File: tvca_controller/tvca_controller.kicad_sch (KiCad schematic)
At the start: 32 parts, among them J1 Programming Header, J2 CAN connector, J3 Batt, J8 Batt, U1 PIC18F26K83, U2 MCP2562, U3 INA180, Y1 Crystal

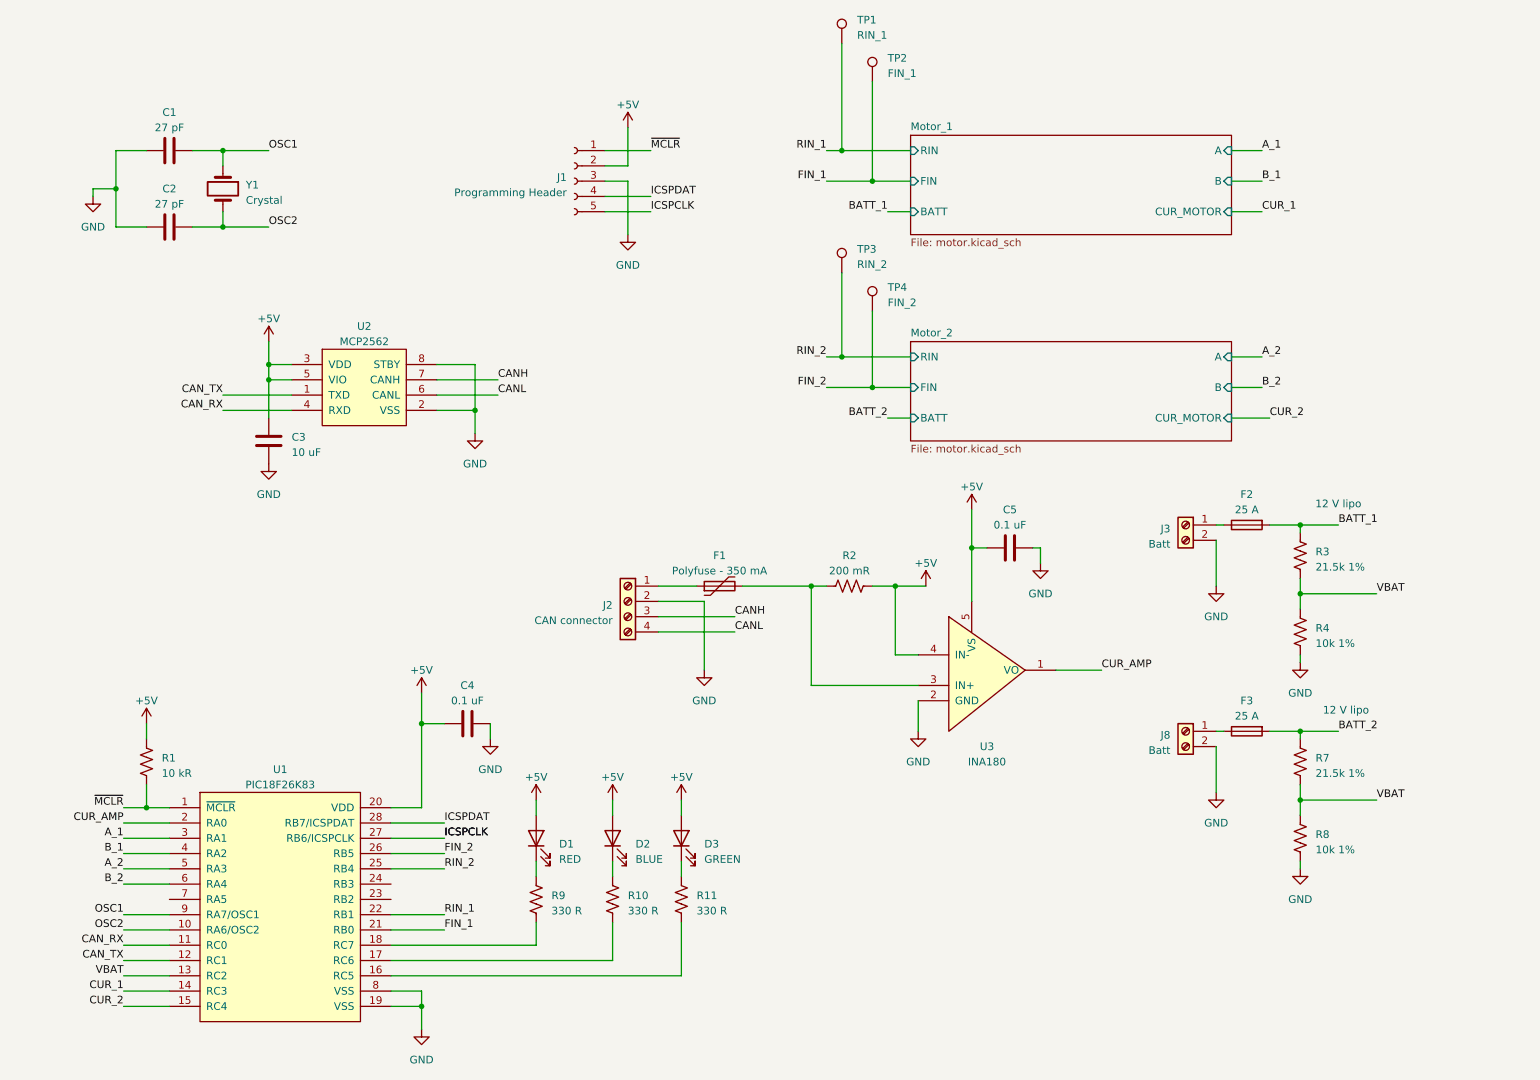
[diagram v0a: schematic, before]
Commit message: Replace motor controller IC
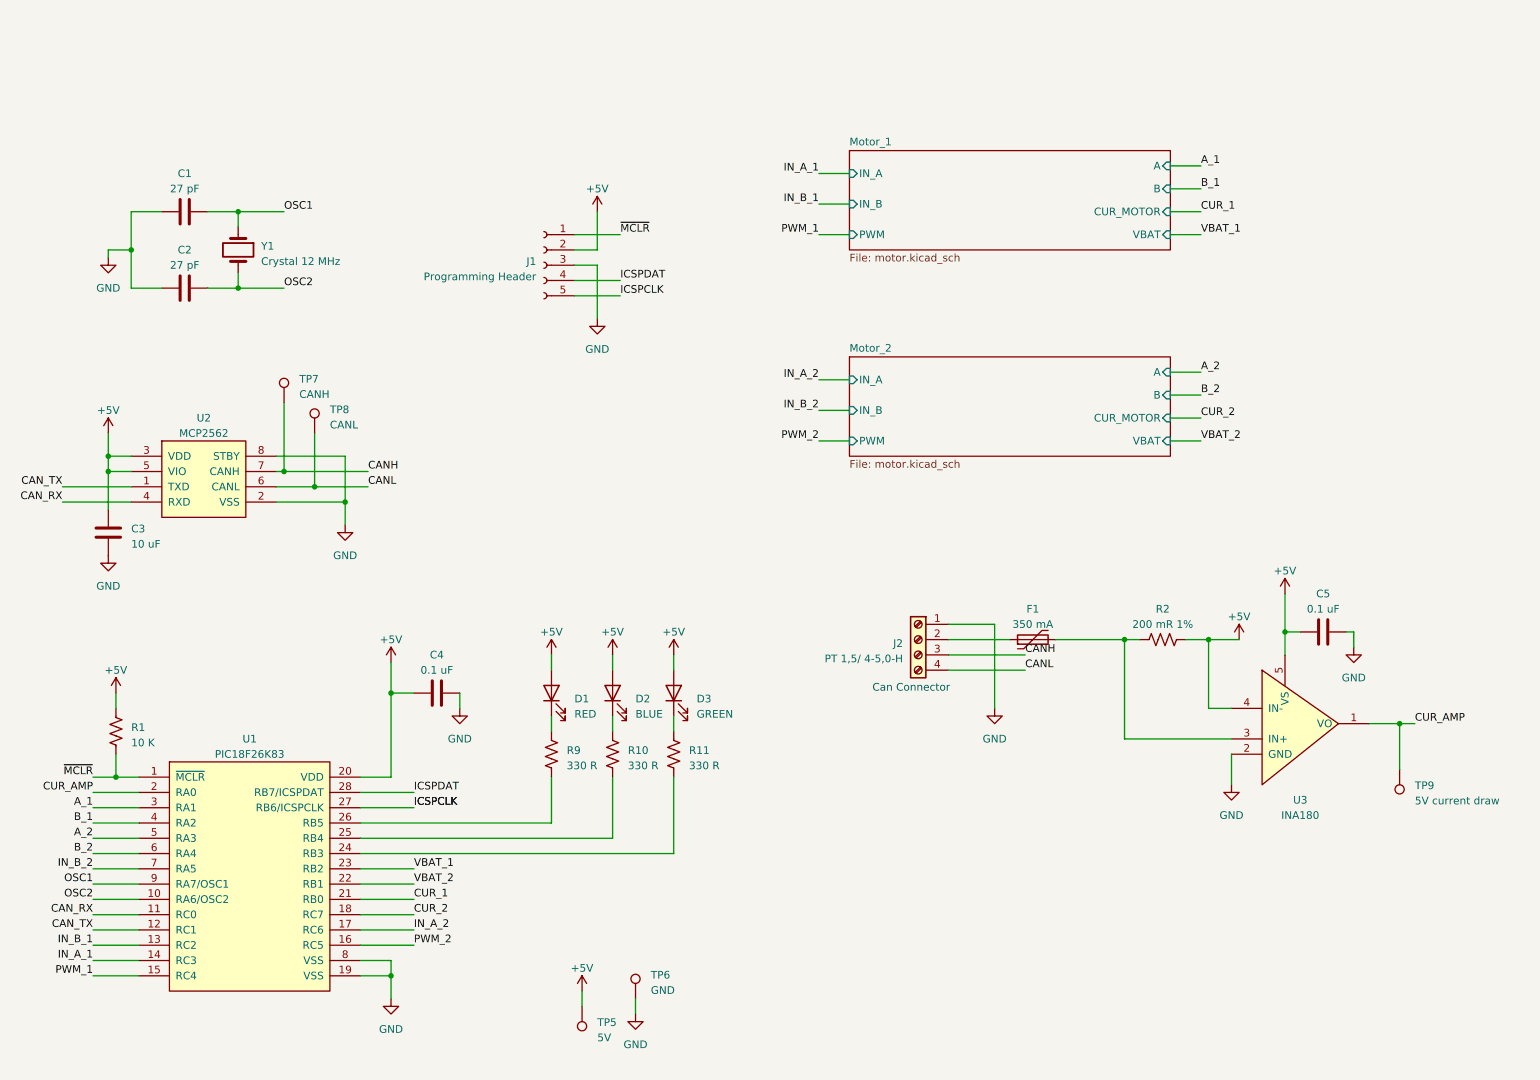
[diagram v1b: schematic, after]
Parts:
- removed F2, F3: 25 A, Fuse:Fuseholder_Cylinder-6.3x32mm_Schurter_0031-8002_Horizontal_Open, symbol Device:Fuse
- removed J3, J8: Batt, canhw_footprints:TE_2-1437667-4, symbol Connector:Screw_Terminal_01x02
- removed R3, R7: 21.5k 1%, Resistor_SMD:R_0805_2012Metric_Pad1.20x1.40mm_HandSolder, symbol Device:R_US
- removed R4, R8: 10k 1%, Resistor_SMD:R_0805_2012Metric_Pad1.20x1.40mm_HandSolder, symbol Device:R_US
- removed TP1: RIN_1, TestPoint:TestPoint_THTPad_2.5x2.5mm_Drill1.2mm, symbol Connector:TestPoint
- removed TP2: FIN_1, TestPoint:TestPoint_THTPad_2.5x2.5mm_Drill1.2mm, symbol Connector:TestPoint
- removed TP3: RIN_2, TestPoint:TestPoint_THTPad_2.5x2.5mm_Drill1.2mm, symbol Connector:TestPoint
- removed TP4: FIN_2, TestPoint:TestPoint_THTPad_2.5x2.5mm_Drill1.2mm, symbol Connector:TestPoint
- added TP5: 5V, TestPoint:TestPoint_THTPad_2.5x2.5mm_Drill1.2mm, symbol Connector:TestPoint
- added TP6: GND, TestPoint:TestPoint_THTPad_2.5x2.5mm_Drill1.2mm, symbol Connector:TestPoint
- added TP7: CANH, TestPoint:TestPoint_THTPad_2.5x2.5mm_Drill1.2mm, symbol Connector:TestPoint
- added TP8: CANL, TestPoint:TestPoint_THTPad_2.5x2.5mm_Drill1.2mm, symbol Connector:TestPoint
- added TP9: 5V current draw, TestPoint:TestPoint_THTPad_2.5x2.5mm_Drill1.2mm, symbol Connector:TestPoint
- F1: value Polyfuse - 350 mA -> 350 mA
- J2: value CAN connector -> PT 1,5/ 4-5,0-H
- R1: value 10 kR -> 10 K
- R2: value 200 mR -> 200 mR 1%
- Y1: value Crystal -> Crystal 12 MHz
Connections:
- net FIN_1 is gone; now on net CUR_1: U1.21 (RB0)
- net FIN_2 is gone; now on an unnamed net: U1.26 (RB5)
- net RIN_2 is gone; now on an unnamed net: U1.25 (RB4)
- net +5V: now also TP5.1
- net CANH: now also TP7.1
- net CANL: now also TP8.1
- net CUR_1: no longer U1.14 (RC3)
- net CUR_2: now also U1.18 (RC7); no longer U1.15 (RC4)
- net CUR_AMP: now also TP9.1
- net GND: now also J2.1 (Pin_1), TP6.1; no longer J2.2 (Pin_2)
- net at F1.1: now also J2.2 (Pin_2); no longer J2.1 (Pin_1)
- net at R9.1: no longer U1.18 (RC7)
- net at R11.1: now also U1.24 (RB3); no longer U1.16 (RC5)
- net at R10.1: no longer U1.17 (RC6)
- net VBAT_1: now reaches U1.23 (RB2)
- net IN_B_2: now reaches U1.7 (RA5)
- net RIN_1 renamed VBAT_2
- net VBAT renamed IN_B_1
- new net IN_A_1: U1.14 (RC3)
- new net IN_A_2: U1.17 (RC6)
- new net PWM_1: U1.15 (RC4)
- new net PWM_2: U1.16 (RC5)
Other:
- sheet Motor_1 ports: added IN_A, IN_B, PWM, VBAT; removed BATT, FIN, RIN
- sheet Motor_2 ports: added IN_A, IN_B, PWM, VBAT; removed BATT, FIN, RIN
- note added: "Can Connector"
- note removed: "12 V lipo"
- moved on the sheet: C1, C2, C3, C4, C5, D1, D2, D3, J1, J2, R1, R10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

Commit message: Update motor controller IC and fuse holders
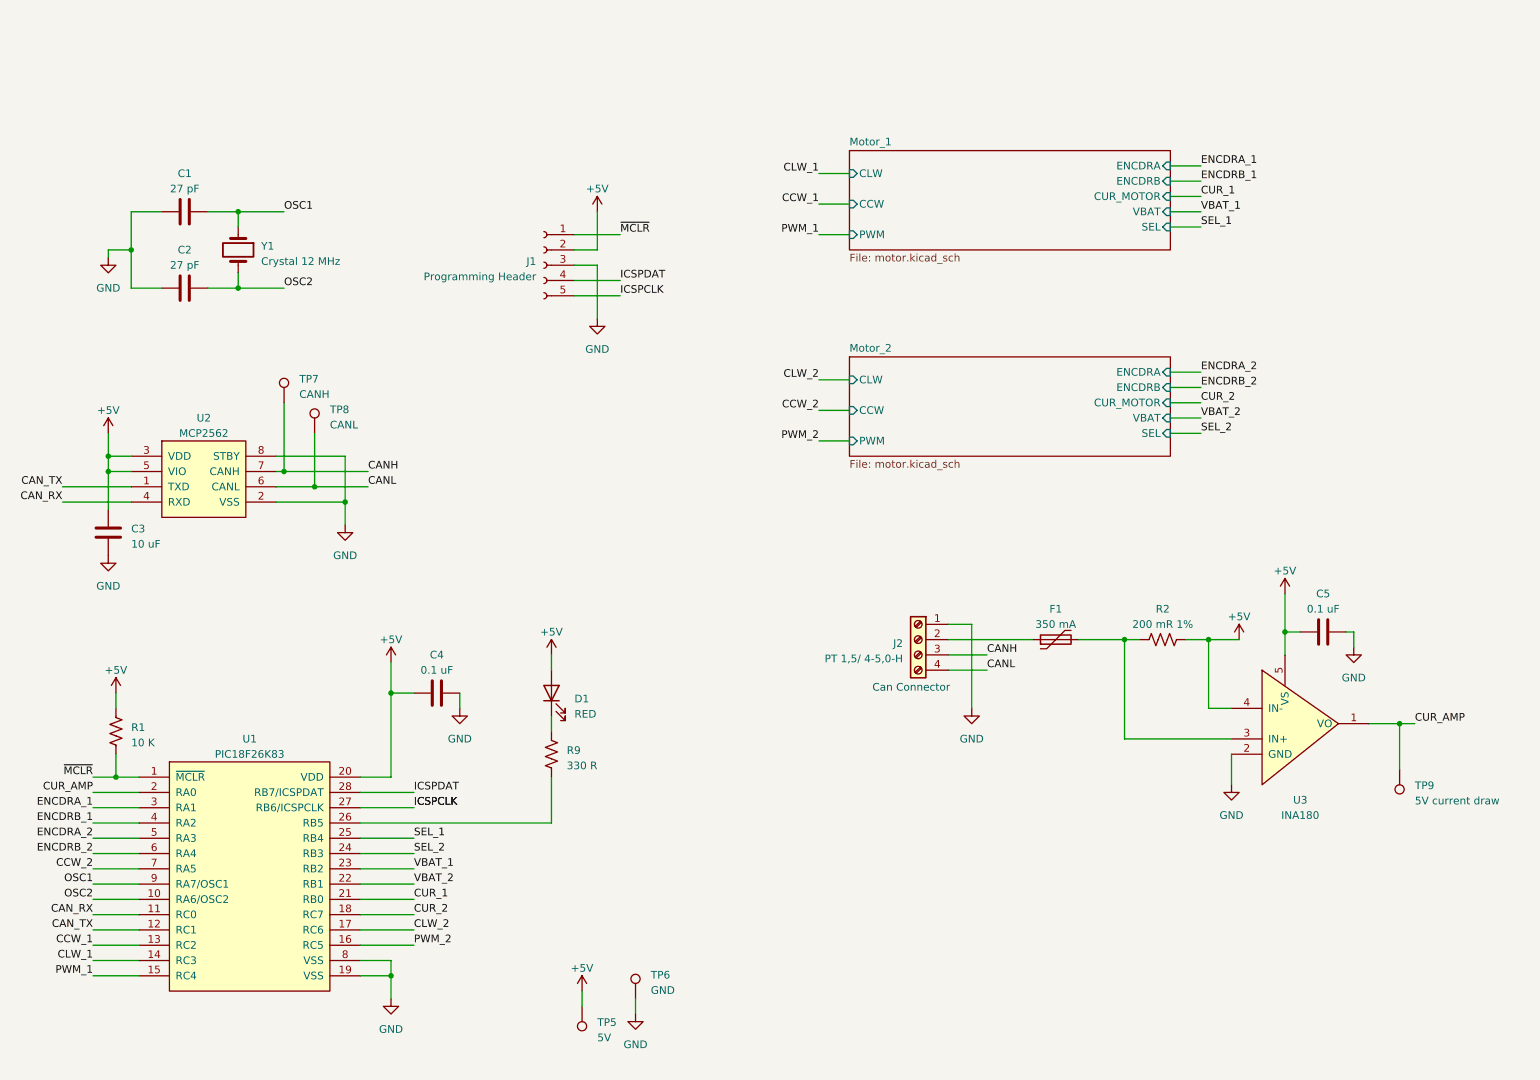
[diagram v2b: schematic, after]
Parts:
- removed D2: BLUE, LED_SMD:LED_0805_2012Metric_Pad1.15x1.40mm_HandSolder, symbol Device:LED
- removed D3: GREEN, LED_SMD:LED_0805_2012Metric_Pad1.15x1.40mm_HandSolder, symbol Device:LED
- removed R10, R11: 330 R, Resistor_SMD:R_0805_2012Metric_Pad1.20x1.40mm_HandSolder, symbol Device:R_US
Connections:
- net SEL_2: now reaches U1.24 (RB3)
- net SEL_1: now reaches U1.25 (RB4)
- net A_1 renamed ENCDRA_1
- net A_2 renamed ENCDRA_2
- net B_1 renamed ENCDRB_1
- net B_2 renamed ENCDRB_2
- net IN_A_1 renamed CLW_1
- net IN_A_2 renamed CLW_2
- net IN_B_1 renamed CCW_1
- net IN_B_2 renamed CCW_2
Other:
- sheet Motor_1 ports: added CCW, CLW, ENCDRA, ENCDRB, SEL; removed A, B, IN_A, IN_B
- sheet Motor_2 ports: added CCW, CLW, ENCDRA, ENCDRB, SEL; removed A, B, IN_A, IN_B
- moved on the sheet: F1

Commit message: Various nit-picks
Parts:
- D1: footprint LED_SMD:LED_0805_2012Metric_Pad1.15x1.40mm_HandSolder -> LED_SMD:LED_1206_3216Metric_Pad1.42x1.75mm_HandSolder
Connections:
- net CANH: now also J2.2 (Pin_2); no longer J2.3 (Pin_3)
- net CANL: now also J2.3 (Pin_3); no longer J2.4 (Pin_4)
- net GND: now also J2.4 (Pin_4); no longer J2.1 (Pin_1)
- net at F1.1: now also J2.1 (Pin_1); no longer J2.2 (Pin_2)
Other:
- moved on the sheet: J2

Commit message: Fix screw terminal
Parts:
- J2: footprint TerminalBlock_Phoenix:TerminalBlock_Phoenix_PT-1,5-4-5.0-H_1x04_P5.00mm_Horizontal -> TerminalBlock_Phoenix:TerminalBlock_Phoenix_MKDS-3-4-5.08_1x04_P5.08mm_Horizontal
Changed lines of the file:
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@@
       (effects (font (size 1.27 1.27)) (justify left))
     )
-    (property "Footprint" "TerminalBlock_Phoenix:TerminalBlock_Phoenix_PT-1,5-4-5.0-H_1x04_P5.00mm_Horizontal" (at 176.53 121.92 0)
+    (property "Footprint" "TerminalBlock_Phoenix:TerminalBlock_Phoenix_MKDS-3-4-5.08_1x04_P5.08mm_Horizontal" (at 176.53 121.92 0)
       (effects (font (size 1.27 1.27)) hide)
     )

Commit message: Fix units/R-sense calculation
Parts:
- C1, C2: value 27 pF -> 27pF
- C3: value 10 uF -> 10uF
- C4, C5: value 0.1 uF -> 0.1uF
- F1: value 350 mA -> 350mA
- R1: value 10 K -> 10k
- R2: value 200 mR 1% -> 200mR 1%
- R9: value 330 R -> 330R
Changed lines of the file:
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@@
       (effects (font (size 1.27 1.27)))
     )
-    (property "Value" "0.1 uF" (at 243.84 114.3 90)
+    (property "Value" "0.1uF" (at 243.84 114.3 90)
       (effects (font (size 1.27 1.27)))
     )
@@
       (effects (font (size 1.27 1.27)))
     )
-    (property "Value" "0.1 uF" (at 96.52 124.46 90)
+    (property "Value" "0.1uF" (at 96.52 124.46 90)
       (effects (font (size 1.27 1.27)))
     )
@@
       (effects (font (size 1.27 1.27)) (justify right))
     )
-    (property "Value" "330 R" (at 118.11 140.335 0)
+    (property "Value" "330R" (at 118.11 140.335 0)
       (effects (font (size 1.27 1.27)) (justify right))
     )
@@
       (effects (font (size 1.27 1.27)))
     )
-    (property "Value" "27 pF" (at 54.61 44.45 90)
+    (property "Value" "27pF" (at 54.61 44.45 90)
       (effects (font (size 1.27 1.27)))
     )
@@
       (effects (font (size 1.27 1.27)) (justify left))
     )
-    (property "Value" "10 K" (at 45.72 136.525 0)
+    (property "Value" "10k" (at 45.72 136.525 0)
       (effects (font (size 1.27 1.27)) (justify left))
     )
@@
       (effects (font (size 1.27 1.27)) (justify left))
     )
-    (property "Value" "10 uF" (at 45.72 103.505 0)
+    (property "Value" "10uF" (at 45.72 103.505 0)
       (effects (font (size 1.27 1.27)) (justify left))
     )
@@
       (effects (font (size 1.27 1.27)))
     )
-    (property "Value" "350 mA" (at 199.39 116.84 90)
+    (property "Value" "350mA" (at 199.39 116.84 90)
       (effects (font (size 1.27 1.27)))
     )
@@
       (effects (font (size 1.27 1.27)))
     )
-    (property "Value" "27 pF" (at 54.61 57.15 90)
+    (property "Value" "27pF" (at 54.61 57.15 90)
       (effects (font (size 1.27 1.27)))
     )
@@
       (effects (font (size 1.27 1.27)))
     )
-    (property "Value" "200 mR 1%" (at 217.17 116.84 90)
-      (effects (font (size 1.27 1.27)))
-    )
+    (property "Value" "200mR 1%" (at 217.17 116.84 90)
+      (effects (font (size 1.27 1.27)))
+    )

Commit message: finalize layout
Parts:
- removed TP5: 5V, TestPoint:TestPoint_THTPad_2.5x2.5mm_Drill1.2mm, symbol Connector:TestPoint
- removed TP6: GND, TestPoint:TestPoint_THTPad_2.5x2.5mm_Drill1.2mm, symbol Connector:TestPoint
- removed TP7: CANH, TestPoint:TestPoint_THTPad_2.5x2.5mm_Drill1.2mm, symbol Connector:TestPoint
- removed TP8: CANL, TestPoint:TestPoint_THTPad_2.5x2.5mm_Drill1.2mm, symbol Connector:TestPoint
- added H1, H2, H3, H4: Mount, MountingHole:MountingHole_3.2mm_M3_Pad, symbol Mechanical:MountingHole_Pad
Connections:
- net GND: now also H1.1, H2.1, H3.1, H4.1

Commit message: add final layout and edge cuts
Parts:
- renumbered TP9 to TP3
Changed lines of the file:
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@@
   (symbol (lib_id "Connector:TestPoint") (at 256.54 140.97 180) (unit 1)
     (in_bom yes) (on_board yes) (dnp no) (fields_autoplaced)
-    (property "Reference" "TP9" (at 259.08 143.637 0)
+    (property "Reference" "TP3" (at 259.08 143.637 0)
       (effects (font (size 1.27 1.27)) (justify right))
     )
@@
       (project "tvca_controller"
         (path "/f08602f6-65d5-48ec-b5dd-079a575e1be0"
-          (reference "TP9") (unit 1)
+          (reference "TP3") (unit 1)
         )
       )

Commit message: routing
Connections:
- net CCW_1: now also U1.23 (RB2); no longer U1.13 (RC2)
- net CLW_1: now also U1.22 (RB1); no longer U1.14 (RC3)
- net CLW_2: now also U1.4 (RA2); no longer U1.17 (RC6)
- net ENCDRA_1: now also U1.24 (RB3); no longer U1.3 (RA1)
- net ENCDRB_1: now also U1.26 (RB5); no longer U1.4 (RA2)
- net SEL_1: now also U1.17 (RC6); no longer U1.25 (RB4)
- net SEL_2: now also U1.14 (RC3); no longer U1.24 (RB3)
- net VBAT_1: now also U1.25 (RB4); no longer U1.23 (RB2)
- net VBAT_2: now also U1.13 (RC2); no longer U1.22 (RB1)
- net at R9.1: now also U1.3 (RA1); no longer U1.26 (RB5)
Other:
- moved on the sheet: C4, D1, R1, R9, U1
